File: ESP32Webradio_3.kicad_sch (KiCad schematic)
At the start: 17 parts, among them J1 5V, J2 Rot, J3 Display, J5 SJ1-3523N, U1 esp32_38_pins-custom_library

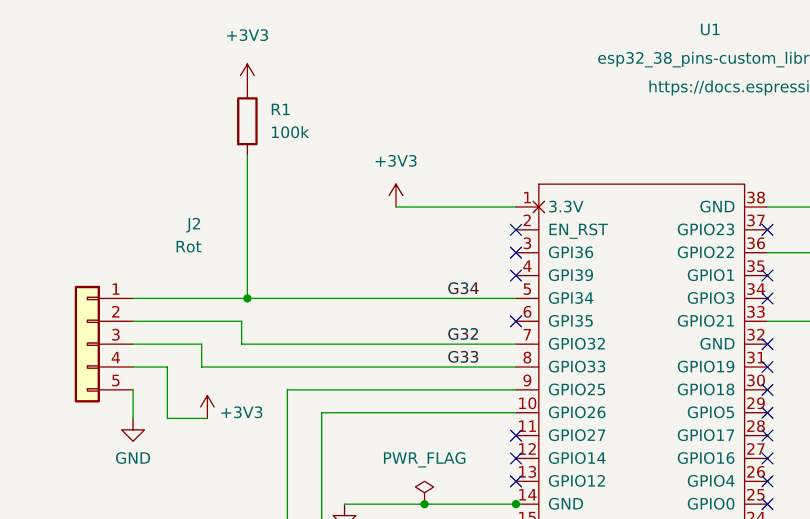
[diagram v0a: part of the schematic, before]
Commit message: flash witout button capacitor added
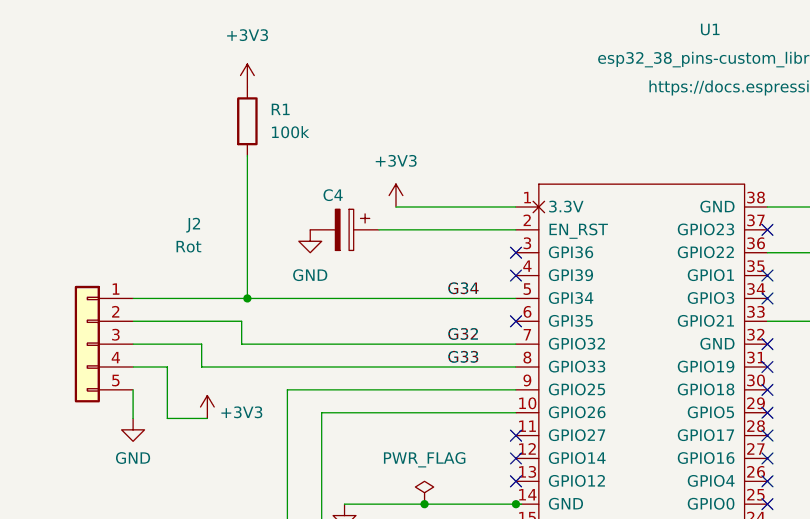
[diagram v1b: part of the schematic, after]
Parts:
- added C4: 10yF, Capacitor_THT:CP_Radial_D4.0mm_P2.00mm, symbol Device:C_Polarized
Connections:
- net GND: now also C4.2
- net at U1.2 (EN_RST): now also C4.1
- no-connect marks 26 -> 25
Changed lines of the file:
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@@
   (no_connect (at 116.205 86.36))
   (no_connect (at 116.205 68.58))
-  (no_connect (at 116.205 58.42))
   (no_connect (at 116.205 60.96))
   (no_connect (at 116.205 63.5))
@@
     (stroke (width 0) (type default) (color 0 0 0 0))
   )
+  (wire (pts (xy 100.965 58.42) (xy 116.205 58.42))
+    (stroke (width 0) (type default) (color 0 0 0 0))
+  )
   (wire (pts (xy 41.275 80.01) (xy 41.275 87.63))
     (stroke (width 0) (type default) (color 0 0 0 0))
@@
     (pin "3")
     (pin "4")
+  )
+  (symbol (lib_id "power:GND") (at 93.345 58.42 0) (unit 1)
+    (in_bom yes) (on_board yes) (fields_autoplaced)
+    (property "Reference" "#PWR0120" (id 0) (at 93.345 64.77 0)
+      (effects (font (size 1.27 1.27)) hide)
+    )
+    (property "Value" "GND" (id 1) (at 93.345 63.5 0))
+    (property "Footprint" "" (id 2) (at 93.345 58.42 0)
+      (effects (font (size 1.27 1.27)) hide)
+    )
+    (property "Datasheet" "" (id 3) (at 93.345 58.42 0)
+      (effects (font (size 1.27 1.27)) hide)
+    )
+    (pin "1")
   )
   (symbol (lib_id "power:GND") (at 261.62 154.305 0) (unit 1)
@@
     (pin "9")
   )
+  (symbol (lib_id "Device:C_Polarized") (at 97.155 58.42 270) (unit 1)
+    (in_bom yes) (on_board yes)
+    (property "Reference" "C4" (id 0) (at 95.885 54.61 90))
+    (property "Value" "10yF" (id 1) (at 98.044 53.34 90)
+      (effects (font (size 1.27 1.27)) hide)
+    )
+    (property "Footprint" "Capacitor_THT:CP_Radial_D4.0mm_P2.00mm" (id 2) (at 93.345 59.3852 0)
+      (effects (font (size 1.27 1.27)) hide)
+    )
+    (property "Datasheet" "~" (id 3) (at 97.155 58.42 0)
+      (effects (font (size 1.27 1.27)) hide)
+    )
+    (pin "1")
+    (pin "2")
+  )
   (symbol (lib_id "Mechanical:MountingHole_Pad") (at 229.87 135.89 0) (unit 1)
     (in_bom yes) (on_board yes) (fields_autoplaced)
@@
       (reference "#PWR0119") (unit 1) (value "GND") (footprint "")
     )
+    (path "/60a7c28c-7f96-44b7-9b73-6d92ad7e3a70"
+      (reference "#PWR0120") (unit 1) (value "GND") (footprint "")
+    )
     (path "/e27b9860-1db7-4cb0-8ed9-3286908a41aa"
       (reference "C1") (unit 1) (value "47pF") (footprint "Capacitor_THT:CP_Radial_D4.0mm_P2.00mm")
@@
       (reference "C3") (unit 1) (value "1000yF") (footprint "Capacitor_THT:CP_Radial_D10.0mm_P2.50mm")
     )
+    (path "/f3ac5656-3097-44af-a50c-c45974c5a3fe"
+      (reference "C4") (unit 1) (value "10yF") (footprint "Capacitor_THT:CP_Radial_D4.0mm_P2.00mm")
+    )
     (path "/ff6a7d87-c5e6-4509-8918-1525dc85be70"

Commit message: clear circuits
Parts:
- J5: footprint CUI_SJ1-3523N -> importedFootprint:CUI_SJ1-3523N
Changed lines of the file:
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@@
       (effects (font (size 1.27 1.27)) (justify right))
     )
-    (property "Footprint" "CUI_SJ1-3523N" (id 2) (at 229.235 114.935 0)
+    (property "Footprint" "importedFootprint:CUI_SJ1-3523N" (id 2) (at 229.235 114.935 0)
       (effects (font (size 1.27 1.27)) (justify left bottom) hide)
     )
@@
     )
     (path "/04b4c05c-20ff-4066-b436-c58a3669d047"
-      (reference "J5") (unit 1) (value "SJ1-3523N") (footprint "CUI_SJ1-3523N")
+      (reference "J5") (unit 1) (value "SJ1-3523N") (footprint "importedFootprint:CUI_SJ1-3523N")
     )
     (path "/8cf50433-5d1e-4e8e-a26a-2df3e5bda93c"
